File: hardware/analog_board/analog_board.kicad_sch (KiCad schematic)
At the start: 2 parts, among them J2 Conn_02x08_Counter_Clockwise, J4 Conn_01x08

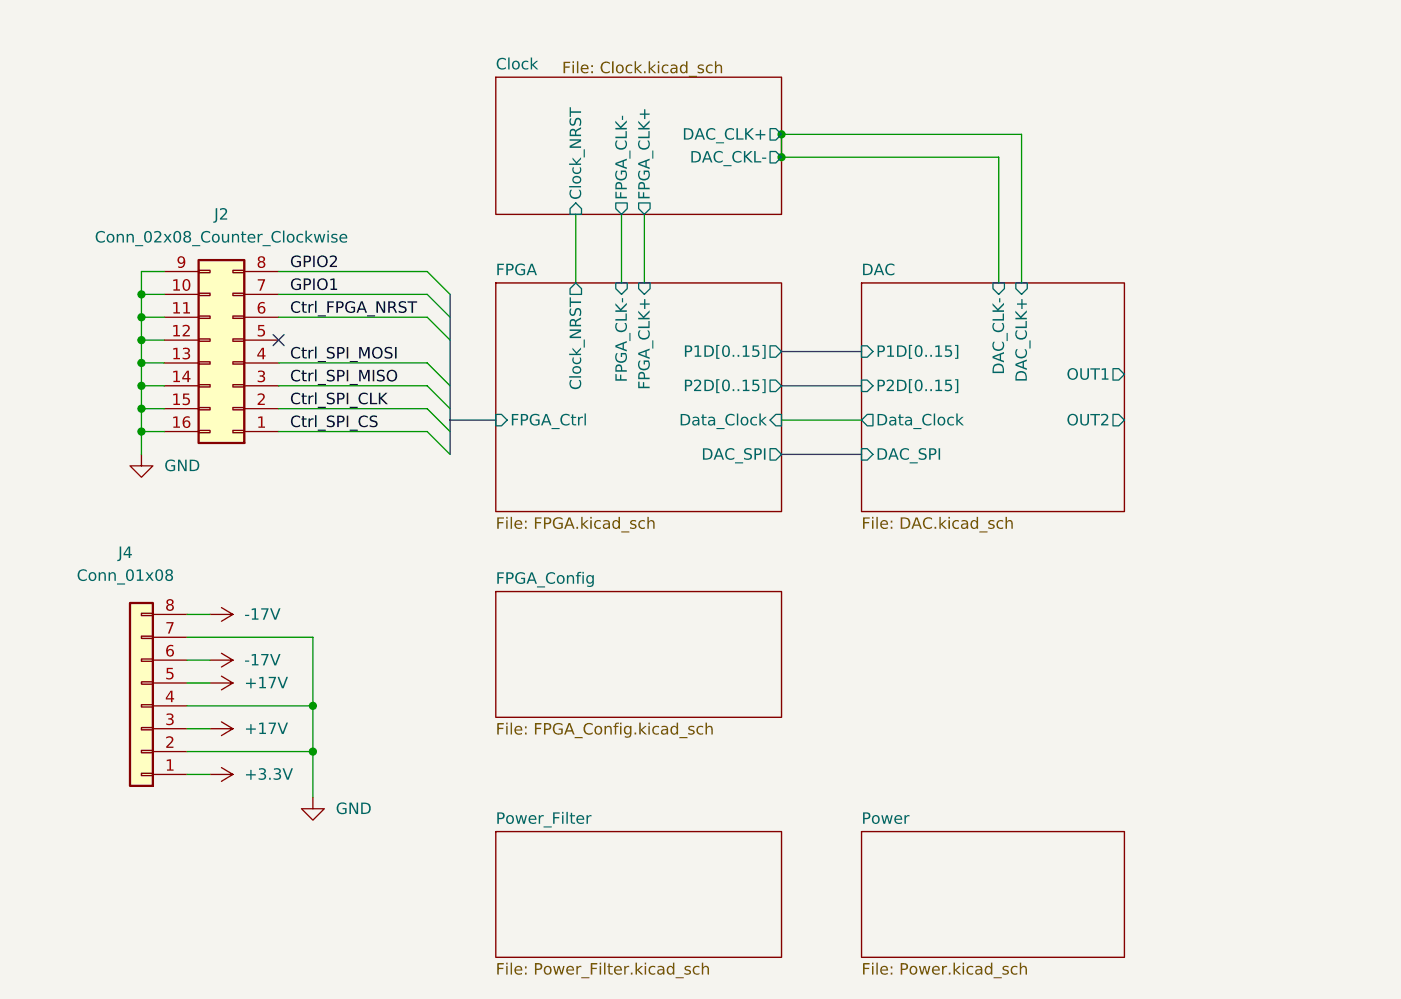
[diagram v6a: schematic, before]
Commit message: feat：根据PCB微调原理图
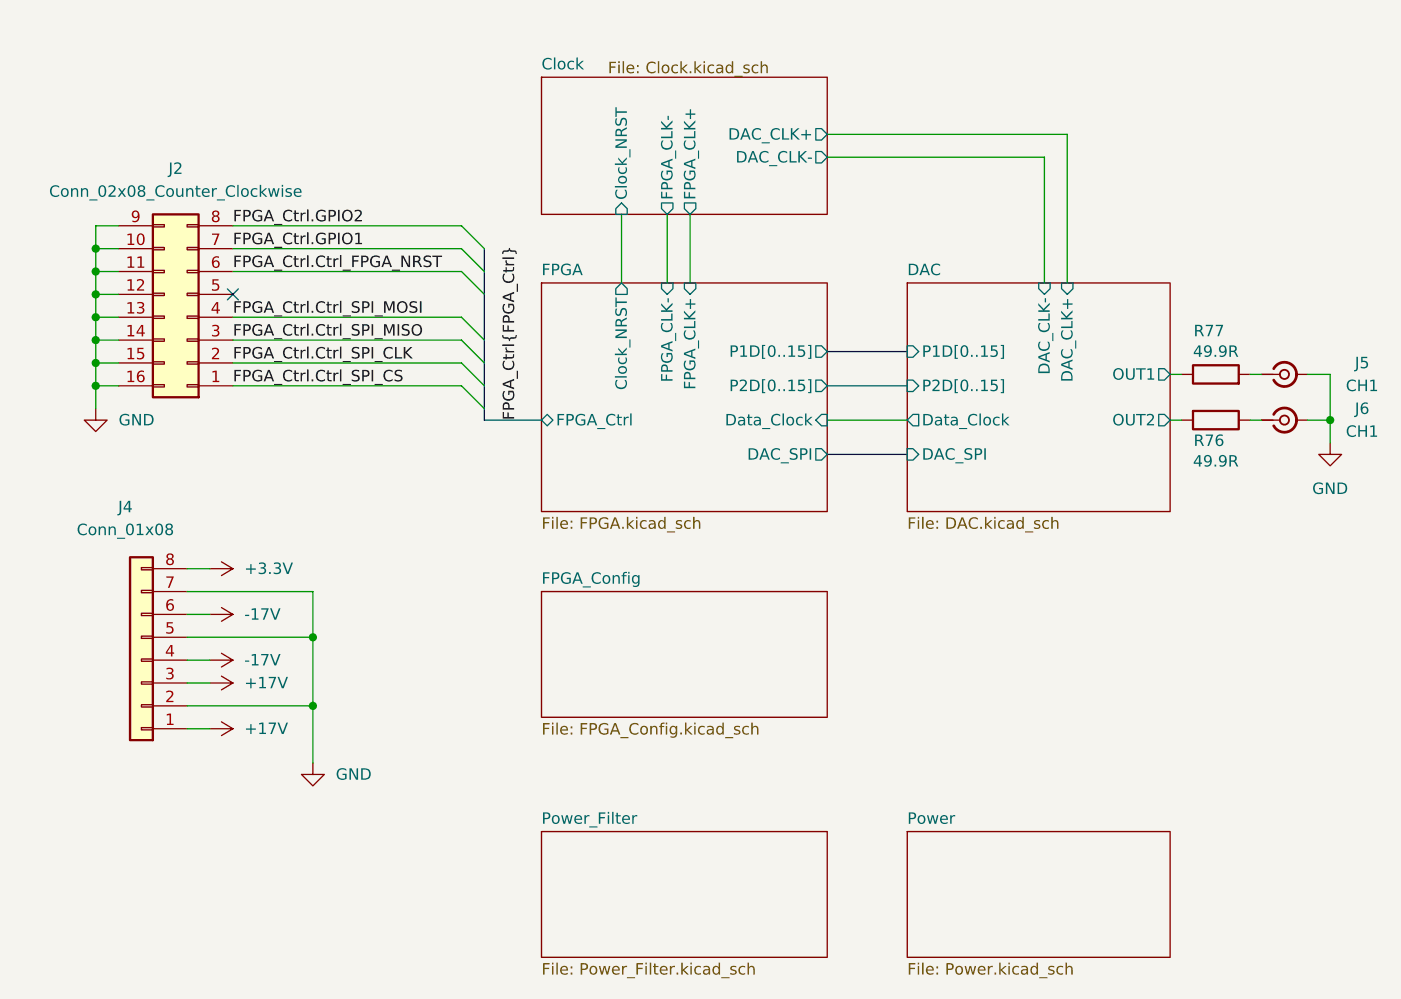
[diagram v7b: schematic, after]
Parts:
- added J5, J6: CH1, Connector_Coaxial:SMA_BAT_Wireless_BWSMA-KWE-Z001, symbol Connector:Conn_Coaxial_Small
- added R76, R77: 49.9R, Resistor_SMD:R_0603_1608Metric, symbol Device:R
- J2: footprint Connector_IDC:IDC-Header_2x08_P2.54mm_Latch_Vertical -> Connector_IDC:IDC_IDC-Header_2x08_P2.54mm_Vertical_antiClockWise
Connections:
- net +17V: now also J4.1 (Pin_1); no longer J4.5 (Pin_5)
- net +3.3V: now also J4.8 (Pin_8); no longer J4.1 (Pin_1)
- net -17V: now also J4.4 (Pin_4); no longer J4.8 (Pin_8)
- net DAC/OUT1: now also R76.1
- net DAC/OUT2: now also R77.2
- net GND: now also J4.5 (Pin_5), J5.2 (Ext), J6.2 (Ext); no longer J4.4 (Pin_4)
- net Ctrl_FPGA_NRST renamed FPGA_Ctrl.Ctrl_FPGA_NRST
- net Ctrl_SPI_CLK renamed FPGA_Ctrl.Ctrl_SPI_CLK
- net Ctrl_SPI_CS renamed FPGA_Ctrl.Ctrl_SPI_CS
- net Ctrl_SPI_MISO renamed FPGA_Ctrl.Ctrl_SPI_MISO
- net Ctrl_SPI_MOSI renamed FPGA_Ctrl.Ctrl_SPI_MOSI
- net GPIO1 renamed FPGA_Ctrl.GPIO1
- net GPIO2 renamed FPGA_Ctrl.GPIO2
- new net: J6.1 (In), R77.1
- new net: J5.1 (In), R76.2
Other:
- sheet Clock ports: added DAC_CLK-; removed DAC_CKL-
- moved on the sheet: J2

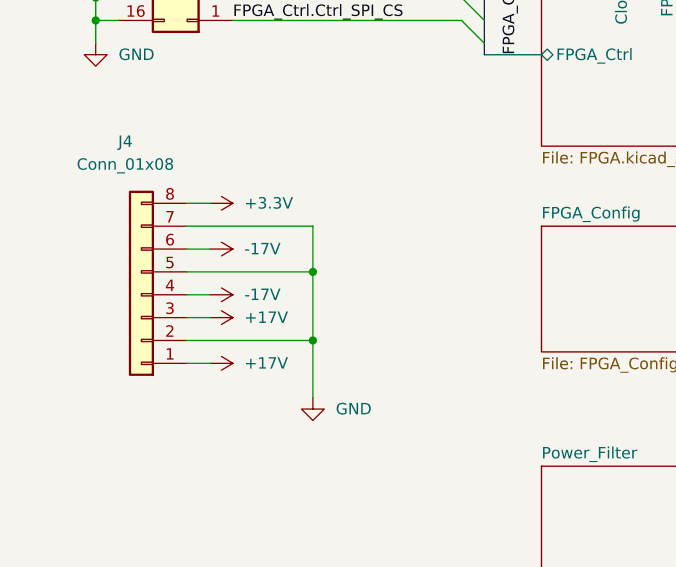
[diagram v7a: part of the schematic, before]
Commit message: feat：DCDC移至控制板
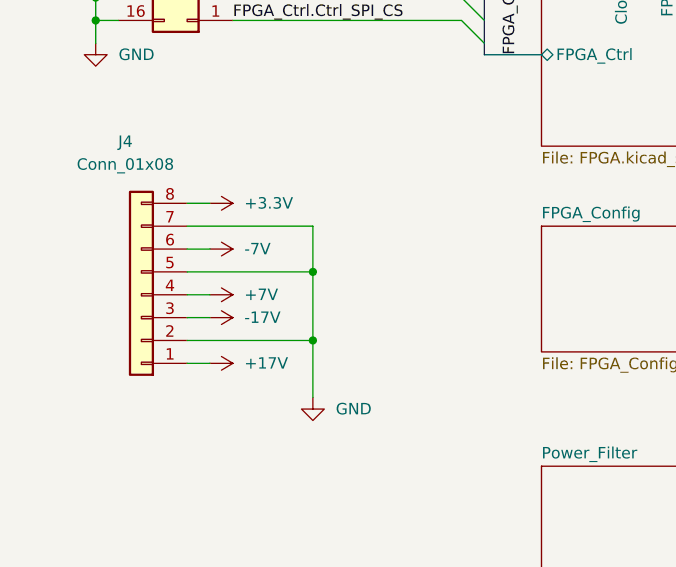
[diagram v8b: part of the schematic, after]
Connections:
- net +17V: no longer J4.3 (Pin_3)
- net -17V: now also J4.3 (Pin_3); no longer J4.4 (Pin_4), J4.6 (Pin_6)
- new net +7V: J4.4 (Pin_4)
- new net -7V: J4.6 (Pin_6)
